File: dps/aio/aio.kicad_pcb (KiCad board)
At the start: 8 copper layers, 35 x 35 mm, 282 parts, among them J201 HD VTX, J301 TYPE-C 16P QTWT, J302 TF-021B-H265, J303 GPS (UART3+I2C1), J304 UART4 (MTF-02P), J305 UART1+UART6 (RX, telemetrie), Q10 DOY180N03T, Q11 DOY180N03T, Q12 DOY180N03T, Q13 DOY180N03T, Q14 DOY180N03T, Q15 DOY180N03T, Q16 DOY180N03T, Q17 DOY180N03T, Q18 DOY180N03T, Q19 DOY180N03T, Q20 DOY180N03T, Q21 DOY180N03T, Q22 DOY180N03T, Q23 DOY180N03T, Q24 DOY180N03T, Q25 DOY180N03T, Q26 DOY180N03T, Q3 DOY180N03T, Q301 AP1606, Q4 DOY180N03T, Q5 DOY180N03T, Q6 DOY180N03T, Q7 DOY180N03T, Q8 DOY180N03T, Q9 DOY180N03T, U13 AT32F421G8U7, U14 NSG2065Q, U15 AT32F421G8U7, U16 NSG2065Q, U17 AT32F421G8U7, U18 NSG2065Q, U19 AT32F421G8U7, U20 NSG2065Q, U201 LMR51430YFDDCR, U24 AIO_outline, U25 INA186A3IDCKR, U3 LMR51430YFDDCR, U301 STM32H743VIH6, U302 SPL06-001 / DPS310, U303 BMI088, U4 LMR51430YFDDCR, U6 LP5912-1.8DRVR, U7 TLV76733DRVR, U8 BMI270, Y301 8MHz 12pF X32258MOB4SI

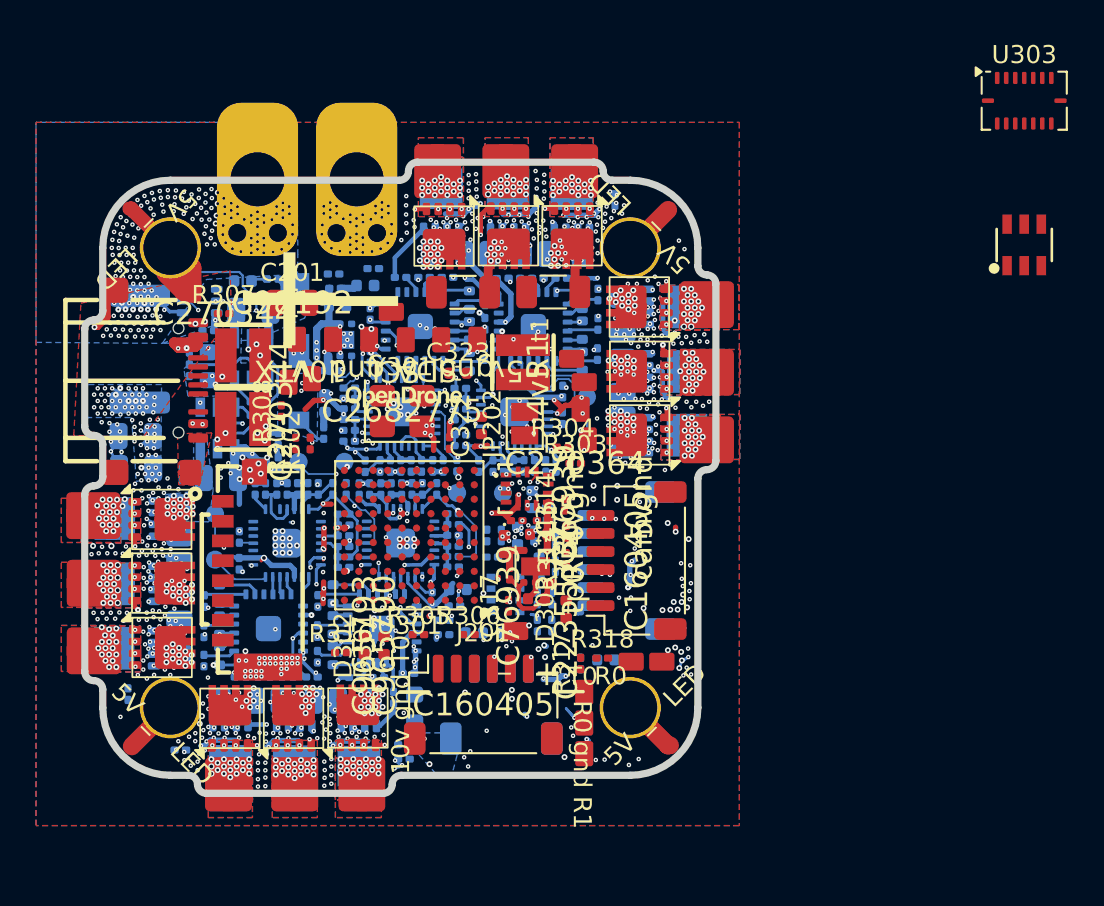
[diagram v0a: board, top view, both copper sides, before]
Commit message: feat: fit every AIO part on the board: switch the VTX off +10V and take an ICM-42688-P as the second IMU
The VTX buck and the BMI088 did not fit; the largest free spot was 2.5 x 2.9 mm.
The VTX now hangs on fc_power's +10V behind a TPS22810 load switch (as OpenAIO
feeds it, but switchable), and the second IMU is an ICM-42688-P on OpenAIO's
LGA-14 footprint. The board update now also carries values and LCSC numbers.

Co-Authored-By: Claude Opus 5.5 <noreply@anthropic.com>
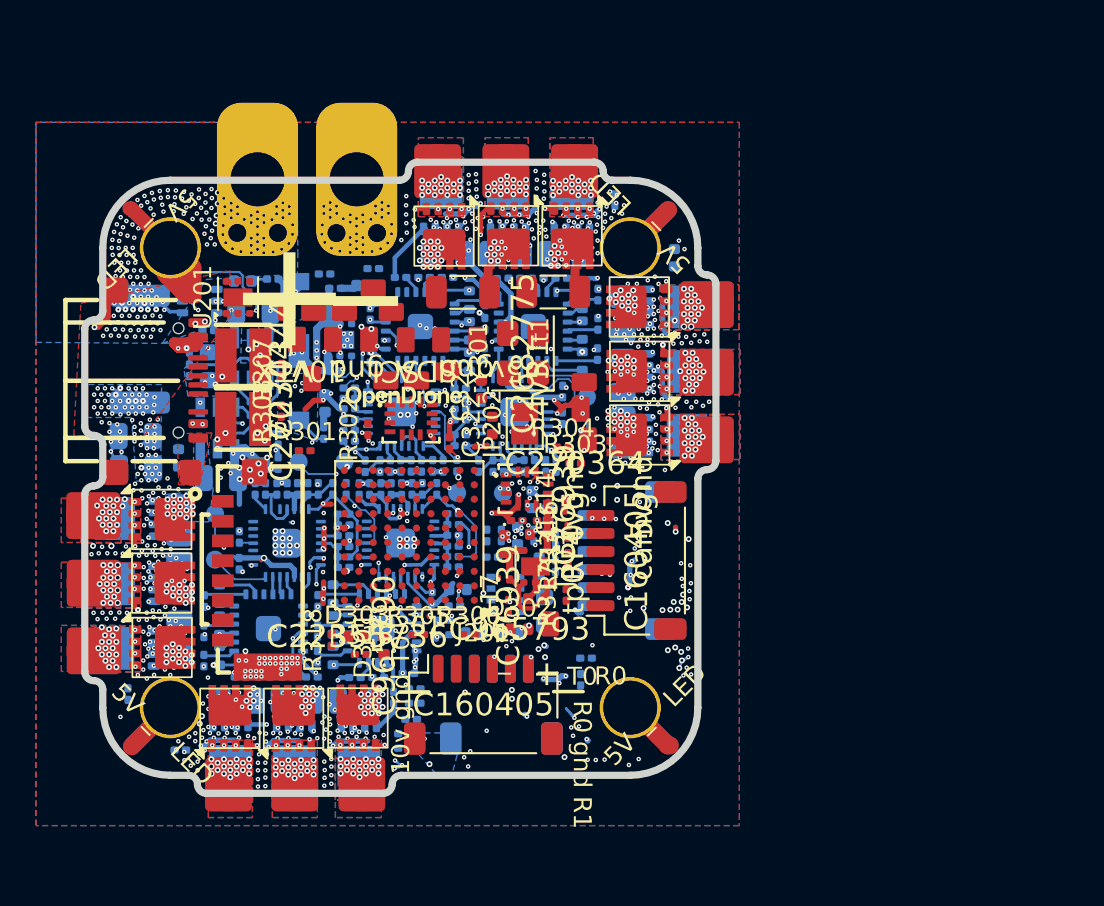
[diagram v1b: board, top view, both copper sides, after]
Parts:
- removed L201: XRTC303020D4R7MBCA, lib:IND-SMD_L3.0-W3.0_AFE303020S
- removed R201: 100k, lib:R_0201_0603Metric
- removed R202: 6.49k, lib:R_0201_0603Metric
- added C324: 10n, lib:C_0201_0603Metric, B.Cu at (73.9, 49.3)
- C201: value 4.7uF 50v -> 1uF 25V; footprint lib:C_0805_2012Metric -> lib:C_0402_1005Metric; moved to B.Cu
- C202: value 100n -> 4.7nF
- C319: value 100n -> 2.2uF
- U201: value LMR51430YFDDCR -> TPS22810DRVR; footprint lib:SOT-23-6_L2.9-W1.6-P0.95-LS2.9-BL -> lib:WSON-6-1EP_2x2mm_P0.65mm_EP1x1.6mm
- U303: value BMI088 -> ICM-42688-P; footprint Package_LGA:Bosch_LGA-16_4.5x3mm_P0.5mm_LayoutBorder7x1y_ClockwisePinNumbering -> lib:LGA-14_L3.0-W2.5-P0.50-BR
- moved U201 43.7 mm to (66.4, 50.9), turned to 90 degrees
- moved U303 38.3 mm to (76.0, 57.6), turned to 180 degrees
- moved R204 30.0 mm to (76.2, 73.4), turned to 0 degrees
- moved TP322 29.7 mm to (69.1, 51.5)
- moved TP321 27.4 mm to (70.6, 51.7)
- moved TP320 26.8 mm to (73.9, 50.4), turned to 90 degrees
- moved C320 25.8 mm to (87.3, 45.5)
- moved R203 23.4 mm to (76.2, 72.6)
- moved C321 22.6 mm to (90.6, 48.7), turned to 90 degrees
- moved TP201 19.6 mm to (76.3, 55.5), turned to 90 degrees
- moved R309 18.6 mm to (76.0, 74.3), turned to 0 degrees
- moved R311 15.6 mm to (60.3, 72.9), turned to 90 degrees
- moved R310 15.5 mm to (75.6, 75.1), turned to 0 degrees
- moved R318 15.0 mm to (71.6, 69.9), turned to 90 degrees
- moved TP317 12.5 mm to (85.8, 58.8), turned to 0 degrees
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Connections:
- C201 pad 1: +BATT -> +10V
- C202 pad 1: /VTX a LD06/SW_VTX -> /VTX a LD06/CT_VTX
- C202 pad 2: /VTX a LD06/CB_VTX -> GND
- U201 pad 1: GND -> /VTX a LD06/+10V_VTX
- U201 pad 2: /VTX a LD06/SW_VTX -> /VTX a LD06/+10V_VTX
- U201 pad 3: +BATT -> /VTX a LD06/CT_VTX
- U201 pad 4: /VTX a LD06/FB_VTX -> GND
- U201 pad 6: /VTX a LD06/CB_VTX -> +10V
- U301 pad A1: /MCU H743/IMU2_ACC_INT -> /MCU H743/IMU2_INT
- U301 pad B1: /MCU H743/IMU2_GYR_INT -> unconnected-(U301-PC15-PadB1)
- U301 pad B6: /MCU H743/IMU2_GYR_CS -> unconnected-(U301-PD5-PadB6)
- U301 pad D7: /MCU H743/IMU2_ACC_CS -> /MCU H743/IMU2_CS
- U303 pad 1: unconnected-(U303-INT2-Pad1) -> /MCU H743/IMU2_MISO
- U303 pad 10: /MCU H743/IMU2_MISO -> GND
- U303 pad 11: +3.3V -> GND
- U303 pad 12: /MCU H743/IMU2_GYR_INT -> /MCU H743/IMU2_CS
- U303 pad 13: unconnected-(U303-INT4-Pad13) -> /MCU H743/IMU2_SCK
- U303 pad 14: /MCU H743/IMU2_ACC_CS -> /MCU H743/IMU2_MOSI
- U303 pad 3: +3.3V -> GND
- U303 pad 4: GND -> /MCU H743/IMU2_INT
- U303 pad 5: /MCU H743/IMU2_GYR_CS -> +3.3V
- U303 pad 8: /MCU H743/IMU2_SCK -> +3.3V
- U303 pad 9: /MCU H743/IMU2_MOSI -> GND
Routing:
- net /MCU H743/UART8_RX: track 3.26 -> 0.00 mm, vias 7 -> 0
- net /MCU H743/PWM10: track 0.00 -> 3.26 mm, vias 0 -> 7
- net GND: track 122.5 -> 121.0 mm, vias 869 -> 856
- net /MCU H743/LED_G: track 0.00 -> 0.69 mm, vias 0 -> 4
- net /LIDAR_PWM: track 0.69 -> 0.00 mm, vias 5 -> 0
- net +3.3V: track 63.6 -> 63.8 mm, vias 64 -> 67
- net Net-(D302-A): vias 0 -> 1
- net /VTX_EN: vias 0 -> 1
- net /VTX a LD06/EN_VTX: vias 2 -> 0
- net /VTX a LD06/+10V_VTX: vias 5 -> 3
- net /MCU H743/UART8_TX: vias 2 -> 0
- net /MCU H743/SD_D3: vias 0 -> 1
- net /MCU H743/SD_D2: vias 1 -> 0
- net /MCU H743/SD_D1: vias 1 -> 0
- net /MCU H743/SD_D0: vias 0 -> 1
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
